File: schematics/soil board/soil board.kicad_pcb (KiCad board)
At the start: 2 copper layers, 65 x 105 mm, 21 parts, among them J1 AVR-ISP-6, U1 ATtiny841-SS, U3 MCP9700Ax-ETT

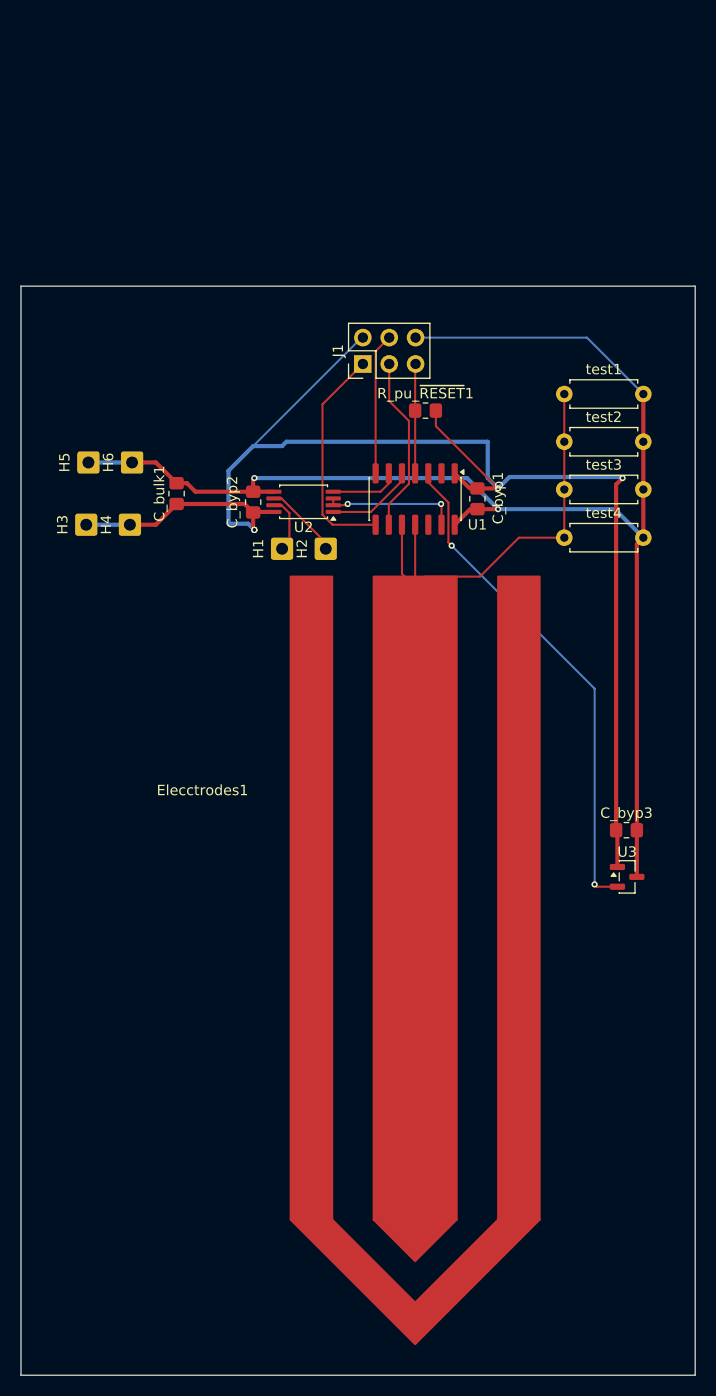
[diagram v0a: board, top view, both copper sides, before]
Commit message: rough draft for a board with capcitive sensor and soil temp sensor, can use rs-485 to communicate
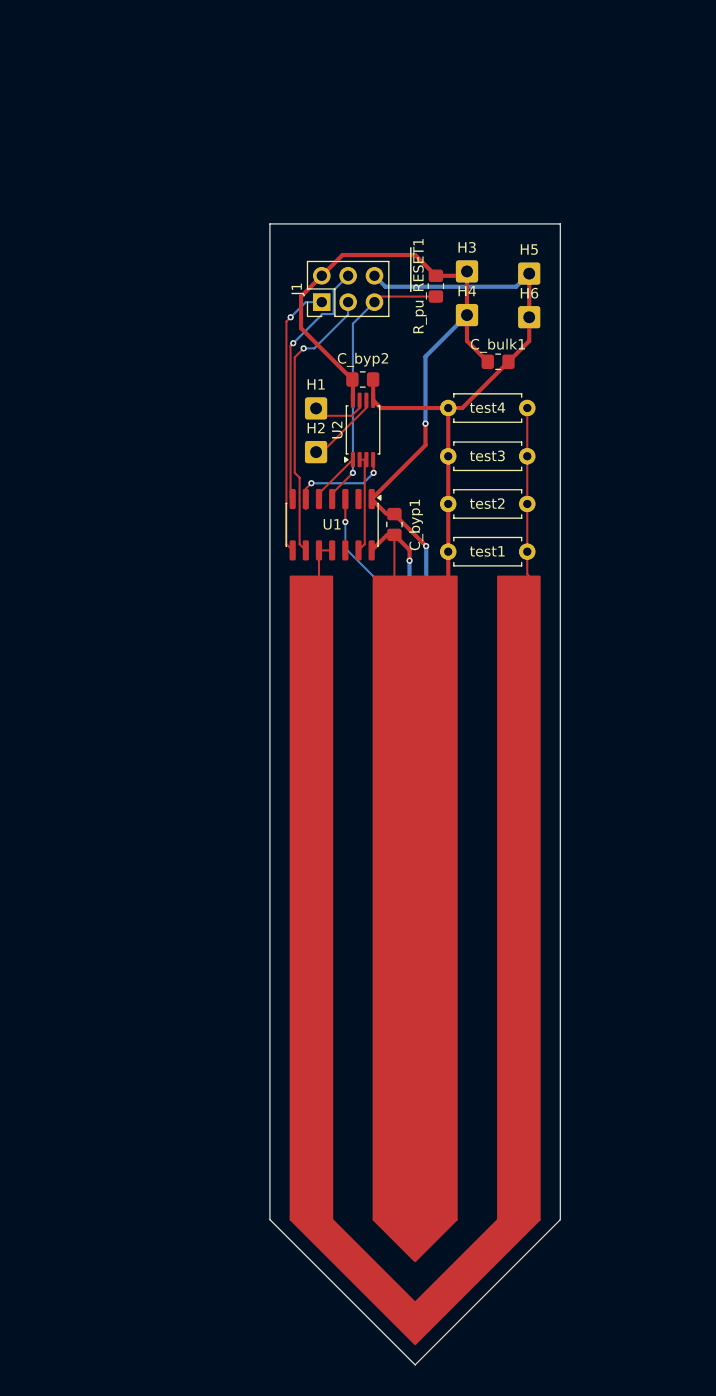
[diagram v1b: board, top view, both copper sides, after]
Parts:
- C_byp3, U3: moved to B.Cu
- moved H5 46.2 mm to (94.0, 83.8), turned to 0 degrees
- moved H3 44.1 mm to (88.0, 83.6), turned to 0 degrees
- moved H6 40.8 mm to (94.0, 88.0), turned to 0 degrees
- moved H4 38.3 mm to (88.0, 87.8), turned to 0 degrees
- moved C_bulk1 33.5 mm to (91.0, 92.3), turned to 0 degrees
- moved U3 20.5 mm to (83.0, 144.0), turned to 90 degrees
- moved C_byp3 20.4 mm to (83.1, 139.5), turned to 180 degrees
- moved C_byp2 15.9 mm to (78.0, 94.0), turned to 0 degrees
- moved test1 15.6 mm to (93.8, 110.6), turned to 180 degrees
- moved H1 13.9 mm to (73.5, 96.8), turned to 0 degrees
- moved test4 13.0 mm to (93.8, 96.8), turned to 180 degrees
- moved R_pu_~{RESET}1 12.0 mm to (85.0, 85.0), turned to 90 degrees
- moved H2 9.37 mm to (73.5, 101.0), turned to 0 degrees
- moved U2 8.99 mm to (78.0, 98.9), turned to 90 degrees
- moved C_byp1 8.37 mm to (81.0, 108.0)
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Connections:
- Elecctrodes1 pad 1: CAP_CHARGE -> GND
- Elecctrodes1 pad 2: floating -> CAP_CHARGE
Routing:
- net +3.3V: track 139.9 -> 104.2 mm, vias 4 -> 2
- net GND: track 136.1 -> 163.4 mm, vias 2 -> 1
- net CAP_CHARGE: track 43.0 -> 22.7 mm
- net ~{RESET}: track 10.6 -> 26.9 mm, vias 0 -> 1
- net MOSI: track 13.6 -> 24.5 mm, vias 0 -> 1
- net SCK: track 17.1 -> 27.3 mm, vias 0 -> 1
- net ADC_11_temp: track 48.6 -> 41.8 mm, vias 2 -> 1
- net MISO: track 21.7 -> 26.5 mm, vias 0 -> 1
- net TXD0_ALT: track 6.66 -> 10.4 mm, vias 0 -> 2
- net DE/~{RE}: track 13.1 -> 9.71 mm, vias 2 -> 0
- net RXD0_ALT: track 8.59 -> 5.87 mm
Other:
- board size 65 x 105 mm -> 28 x 110 mm

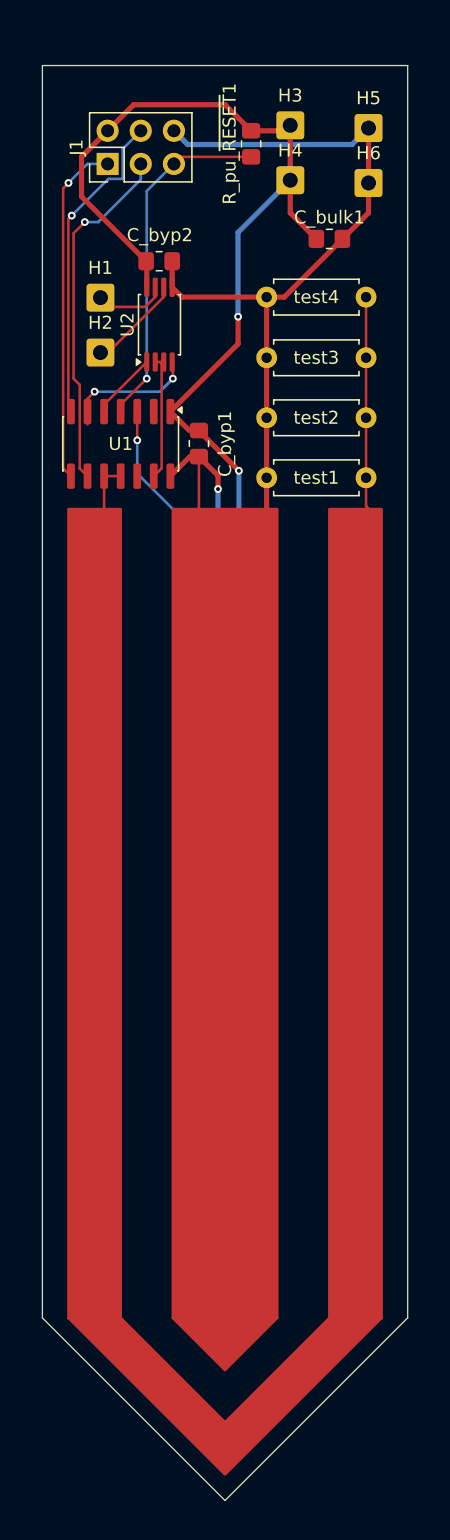
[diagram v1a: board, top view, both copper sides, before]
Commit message: Changed connectors for rs-485
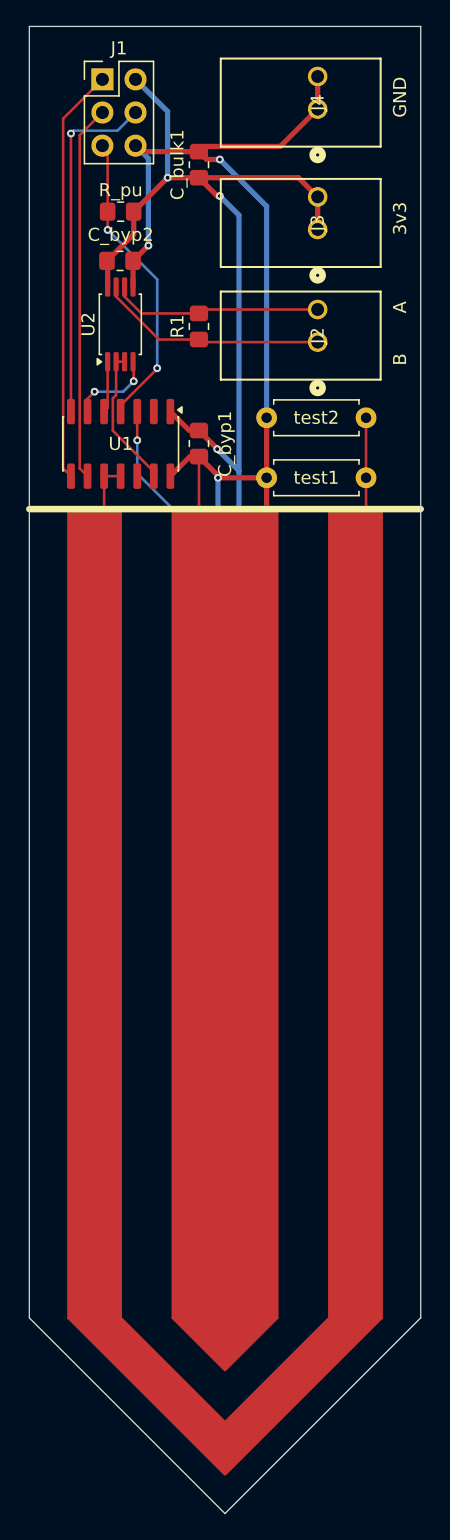
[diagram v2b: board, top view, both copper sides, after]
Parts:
- removed H1, H2, H3, H4, H5, H6: MountingHole_Pad, Connector_Wire:SolderWire-0.5sqmm_1x01_D0.9mm_OD2.1mm
- removed test3, test4: R_US, Resistor_THT:R_Axial_DIN0207_L6.3mm_D2.5mm_P7.62mm_Horizontal
- added J2: 1989748, footprints:CONN_1989748_PXC, F.Cu at (90.1, 100.2)
- added J3: 1989748, footprints:CONN_1989748_PXC, F.Cu at (90.1, 91.6)
- added J4: 1989748, footprints:CONN_1989748_PXC, F.Cu at (90.1, 82.3)
- added R1: R_US, Resistor_SMD:R_0805_2012Metric_Pad1.20x1.40mm_HandSolder, F.Cu at (81.0, 99.0)
- moved C_bulk1 11.5 mm to (81.0, 86.6), turned to 90 degrees
- moved R_pu 11.3 mm to (75.0, 90.2), turned to 0 degrees
- moved J1 6.49 mm to (73.6, 80.1), turned to 0 degrees
- moved C_byp2 3.00 mm to (75.0, 94.0)
- moved U2 3.00 mm to (75.0, 98.8)
- renumbered R_pu_~{RESET}1 to R_pu
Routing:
- net Net-(U2-B): track 5.55 -> 17.6 mm
- net CAP_CHARGE: track 22.7 -> 13.1 mm
- net Net-(U2-A): track 7.35 -> 16.2 mm
- net MISO: track 26.5 -> 31.9 mm, vias 1 -> 0
- net GND: track 163.4 -> 168.3 mm, vias 1 -> 3
- net +3.3V: track 104.2 -> 99.7 mm, vias 2 -> 3
- net TXD0_ALT: track 10.4 -> 6.60 mm
- net MOSI: track 24.5 -> 27.2 mm
- net ~{RESET}: track 26.9 -> 24.6 mm, vias 1 -> 2
- net SCK: track 27.3 -> 28.8 mm, vias 1 -> 0
- net DE/~{RE}: track 9.71 -> 10.8 mm
- net RXD0_ALT: track 5.87 -> 5.19 mm
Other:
- board size 28 x 110 mm -> 30 x 114 mm
- board text added: "3v3"
- board text added: "A"
- board text added: "B"
- board text added: "GND"

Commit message: Interface for temp sensor and soil moisture sensor
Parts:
- removed Elecctrodes1: C, soil_cap:Untitled
- removed J3, J4: 1989748, footprints:CONN_1989748_PXC
- removed R_pu: 10k, Resistor_SMD:R_0805_2012Metric_Pad1.20x1.40mm_HandSolder
- removed test1, test2: R_US, Resistor_THT:R_Axial_DIN0207_L6.3mm_D2.5mm_P7.62mm_Horizontal
- added J5: 54602-908LF, 54602_908LF_footprints:CONN8_2-908LF_AMP, F.Cu at (97.0, 74.7)
- added PWR1: LED, LED_SMD:LED_0805_2012Metric_Pad1.15x1.40mm_HandSolder, F.Cu at (88.6, 82.3)
- added R2: 56, Resistor_SMD:R_0805_2012Metric_Pad1.20x1.40mm_HandSolder, F.Cu at (96.8, 82.4)
- added R3: 56, Resistor_SMD:R_0805_2012Metric_Pad1.20x1.40mm_HandSolder, F.Cu at (99.6, 97.4)
- added R_pu_~{RESET}1: 10k, Resistor_SMD:R_0805_2012Metric_Pad1.20x1.40mm_HandSolder, F.Cu at (87.3, 107.0)
- added TEST1: LED, LED_SMD:LED_0805_2012Metric_Pad1.15x1.40mm_HandSolder, F.Cu at (98.6, 100.4)
- C_byp3, U3: moved to F.Cu
- J2: value 1989748 -> Conn_01x03_Pin; footprint footprints:CONN_1989748_PXC -> Connector_PinHeader_2.54mm:PinHeader_1x03_P2.54mm_Vertical
- R1: value R_US -> 120; moved to B.Cu
- moved J1 33.9 mm to (90.2, 109.6), turned to 90 degrees
- moved C_byp2 19.3 mm to (92.7, 86.4)
- moved U1 19.3 mm to (92.7, 100.4), turned to 0 degrees
- moved R1 19.2 mm to (92.7, 83.8), turned to 0 degrees
- moved U2 19.2 mm to (92.7, 91.6)
- moved C_byp1 14.3 mm to (87.9, 95.5), turned to 90 degrees
- moved C_bulk1 12.9 mm to (92.7, 81.3), turned to 0 degrees
- moved C_byp3 12.8 mm to (92.7, 148.0), turned to 0 degrees
- moved U3 12.7 mm to (92.7, 152.1), turned to 0 degrees
- moved J2 8.23 mm to (83.3, 95.6), turned to 0 degrees
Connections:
- J2 pad 1: Net-(U2-B) -> GND
- J2 pad 2: Net-(U2-A) -> ADC_10_moisture
- U1 pad 10: CAP_CHARGE -> unconnected-(U1-PA3-Pad10)
- U1 pad 11: CAP_CHARGE -> Net-(TEST1-A)
- U1 pad 12: unconnected-(U1-PA1-Pad12) -> /RE
- U1 pad 13: DE/~{RE} -> DE
- U1 pad 2: unconnected-(U1-XTAL1/PB0-Pad2) -> ADC_11_temp
- U1 pad 3: ADC_11_temp -> ADC_10_moisture
- U2 pad 2: DE/~{RE} -> /RE
- U2 pad 3: DE/~{RE} -> DE
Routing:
- net GND: track 168.3 -> 5.08 mm, vias 3 -> 5
- net MISO: track 31.9 -> 8.53 mm, vias 0 -> 1
- net MOSI: track 27.2 -> 4.22 mm, vias 1 -> 0
- net SCK: track 28.8 -> 10.5 mm, vias 0 -> 1
- net +3.3V: track 99.7 -> 81.6 mm
- net ADC_11_temp: track 41.8 -> 59.9 mm, vias 1 -> 2
- net CAP_CHARGE: track 13.1 -> 0.00 mm
- net DE/~{RE}: track 10.8 -> 0.00 mm
- net Net-(PWR1-K): track 0.00 -> 8.22 mm
- net ADC_10_moisture: track 0.00 -> 7.43 mm, vias 0 -> 1
- net /RE: track 0.00 -> 6.44 mm
- net ~{RESET}: track 24.6 -> 19.1 mm, vias 2 -> 0
- net DE: track 0.00 -> 4.87 mm
- net TXD0_ALT: track 6.60 -> 10.6 mm
- net RXD0_ALT: track 5.19 -> 8.62 mm, vias 0 -> 2
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- added copper zone on B.Cu, net +3.3V
- added copper zone on F.Cu, net +3.3V
- added copper zone on B.Cu, net GND
- added copper zone on F.Cu, net GND
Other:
- board size 30 x 114 mm -> 23.6 x 96.8 mm
- board text added: "+"
- board text added: "-"
- board text removed: "3v3"
- board text removed: "A"
- board text removed: "B"
- board text removed: "GND"

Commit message: Final changes to pcbs before ordering
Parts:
- renumbered C_bulk1 to C1, C_byp1 to C2, C_byp2 to C3, C_byp3 to C4, J5 to J2, J2 to J3, R_pu_~{RESET}1 to R1, R3 to R2, R2 to R3, R1 to R4
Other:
- board text added: "3.3v MOSI GND MISO SCK RES"
